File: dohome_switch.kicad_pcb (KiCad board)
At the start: 2 copper layers, 48.3 x 22.9 mm, 25 parts, among them P1 FTDI, P2 CONN_02X08, Q1 BSS138, Q2 BSS138, SW1 RST/PRG, U1 RT9013-33GB, U2 ESP-12E, U3 WS2812B

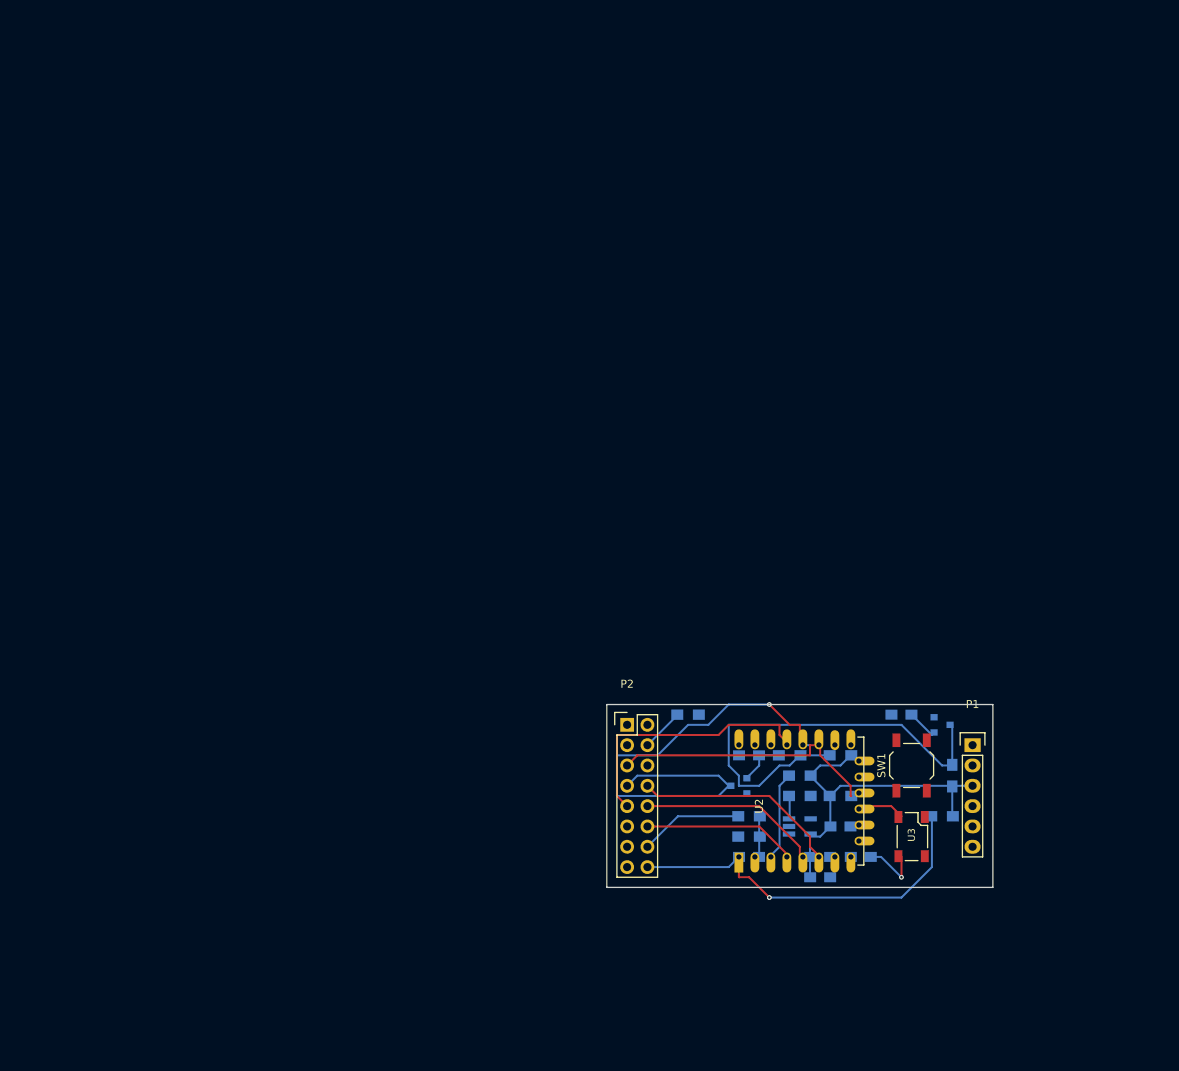
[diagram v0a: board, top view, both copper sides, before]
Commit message: CODE: new version with ftdi
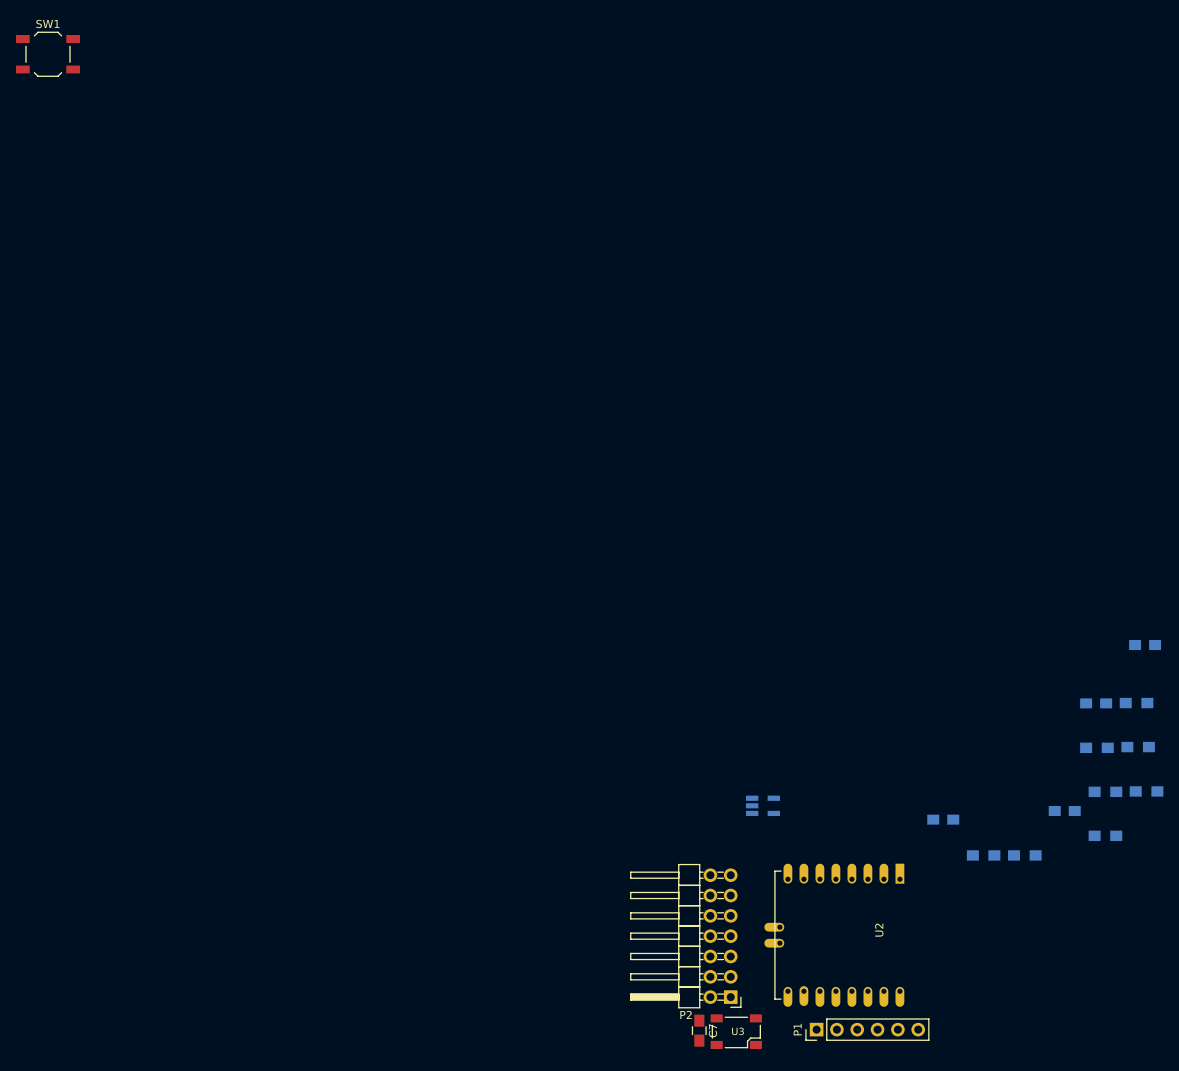
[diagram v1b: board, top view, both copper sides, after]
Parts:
- removed C3: 0.1uF, Capacitors_SMD:C_0805_HandSoldering
- removed C5: 2u2, Capacitors_SMD:C_0805_HandSoldering
- removed Q1, Q2: BSS138, TO_SOT_Packages_SMD:SOT-23
- removed R6: 470k, Resistors_SMD:R_0805_HandSoldering
- removed R7: 100k, Resistors_SMD:R_0805_HandSoldering
- C7: moved to F.Cu
- P1: footprint Pin_Headers:Pin_Header_Straight_1x06 -> Socket_Strips:Socket_Strip_Straight_1x06_Pitch2.54mm
- P2: value CONN_02X08 -> CONN_02X07; footprint Pin_Headers:Pin_Header_Straight_2x08 -> Pin_Headers:Pin_Header_Angled_2x07_Pitch2.54mm
- moved SW1 139.8 mm to (0.00, 0.00), turned to 0 degrees
- moved R10 54.3 mm to (132.2, 97.7)
- moved C2 49.9 mm to (137.1, 73.8)
- moved R9 49.9 mm to (136.3, 86.6)
- moved C1 47.4 mm to (131.0, 81.1)
- moved R2 43.4 mm to (137.3, 92.1)
- moved P1 40.6 mm to (96.1, 121.9), turned to 90 degrees
- moved R5 38.8 mm to (136.1, 81.1)
- moved P2 36.4 mm to (85.3, 117.9), turned to 180 degrees
- moved U3 32.8 mm to (86.0, 122.2), turned to 0 degrees
- moved R4 32.1 mm to (131.1, 86.7)
- moved R8 29.7 mm to (117.0, 100.1)
- moved C7 29.7 mm to (81.4, 122.0), turned to 270 degrees
- moved R1 29.1 mm to (122.1, 100.1)
- moved C6 28.1 mm to (127.1, 94.6)
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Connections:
- C1 pad 1: Net-(C1-Pad1) -> +5V
- C1 pad 2: Net-(C1-Pad2) -> GND
- C2 pad 2: Net-(C2-Pad2) -> GND
- C4 pad 2: Net-(C4-Pad2) -> GND
- C6 pad 2: Net-(C6-Pad2) -> GND
- C7 pad 1: Net-(C7-Pad1) -> +5V
- C7 pad 2: Net-(C7-Pad2) -> GND
- P1 pad 1: Net-(P1-Pad1) -> +3V3
- P1 pad 2: Net-(P1-Pad2) -> /GPIO0
- P1 pad 3: +3V3 -> /RXD
- P1 pad 4: /RXD -> /TXD
- P1 pad 5: /TXD -> GND
- P1 pad 6: Net-(P1-Pad6) -> /RESET
- P2 pad 1: Net-(P2-Pad1) -> GND
- P2 pad 11: /GPIO5 -> /GPIO12
- P2 pad 12: /GPIO16 -> /GPIO13
- P2 pad 13: /RXD -> +3V3
- P2 pad 14: /A0 -> +5V
- P2 pad 2: +3V3 -> /GPIO15
- P2 pad 3: Net-(P2-Pad3) -> /GPIO2
- P2 pad 4: /GPIO15 -> /GPIO0
- P2 pad 5: /GPIO2 -> /GPIO4
- P2 pad 6: /GPIO13 -> /GPIO5
- P2 pad 7: /GPIO0 -> /GPIO10
- P2 pad 8: /GPIO12 -> /A0
- P2 pad 9: /GPIO4 -> /GPIO16
- R1 pad 1: Net-(R1-Pad1) -> +5V
- R1 pad 2: Net-(R1-Pad2) -> GND
- R10 pad 2: Net-(R10-Pad2) -> GND
- R9 pad 2: Net-(R9-Pad2) -> GND
- SW1 pad 1: Net-(C3-Pad1) -> GND
- U1 pad 1: Net-(C1-Pad1) -> +5V
- U1 pad 2: Net-(U1-Pad2) -> GND
- U1 pad 3: Net-(R1-Pad1) -> +5V
- U1 pad 4: Net-(U1-Pad4) -> (no net)
- U2 pad 9: Net-(U2-Pad9) -> GND
- U3 pad 1: Net-(C7-Pad1) -> +5V
- U3 pad 2: Net-(U3-Pad2) -> (no net)
- U3 pad 3: Net-(U3-Pad3) -> GND
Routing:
- net /GPIO0: track 68.7 -> 0.00 mm, vias 1 -> 0
- net Net-(Q1-Pad3): track 52.8 -> 0.00 mm
- net /RESET: track 51.7 -> 0.00 mm, vias 1 -> 0
- net +3V3: track 45.2 -> 0.00 mm
- net /GPIO2: track 34.3 -> 0.00 mm
- net /GPIO4: track 33.7 -> 0.00 mm
- net /GPIO12: track 26.2 -> 0.00 mm
- net /GPIO14: track 22.8 -> 0.00 mm
- net /GPIO16: track 19.7 -> 0.00 mm
- net /A0: track 12.9 -> 0.00 mm
- net /CH_PD: track 11.5 -> 0.00 mm
- net Net-(C7-Pad1): track 7.81 -> 0.00 mm, vias 1 -> 0
- net /GPIO9: track 6.43 -> 0.00 mm
- net Net-(C5-Pad2): track 5.98 -> 0.00 mm
- net /ADC: track 5.86 -> 0.00 mm
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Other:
- board outline removed

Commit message: CODE: Without lines
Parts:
- removed SW1: RST/PRG, Buttons_Switches_SMD:SW_SPST_TL3342
- added JP1: JP1, Pin_Headers:Pin_Header_Straight_1x02_Pitch2.54mm, F.Cu at (89.3, 105.2)
- moved C1 51.4 mm to (88.3, 109.7), turned to 270 degrees
- moved C2 51.3 mm to (97.5, 106.4), turned to 90 degrees
- moved R5 48.5 mm to (100.2, 113.7), turned to 90 degrees
- moved R10 42.1 mm to (93.9, 115.3), turned to 180 degrees
- moved R2 40.2 mm to (99.8, 106.4), turned to 270 degrees
- moved R4 39.5 mm to (102.4, 113.7), turned to 90 degrees
- moved R9 37.8 mm to (103.9, 106.1)
- moved C6 35.3 mm to (96.1, 111.6), turned to 180 degrees
- moved R3 33.5 mm to (103.9, 110.2), turned to 180 degrees
- moved R1 33.2 mm to (90.4, 109.7), turned to 270 degrees
- moved C4 21.1 mm to (96.1, 109.7), turned to 180 degrees
- moved R8 15.2 mm to (103.9, 108.1)
- moved U1 13.0 mm to (93.9, 106.2)
- moved U2 0.89 mm to (107.4, 103.2)
- moved P1 0.71 mm to (96.8, 122.0)
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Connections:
- C1 pad 1: +5V -> /PWR
- C7 pad 1: +5V -> /PWR
- P1 pad 1: +3V3 -> /PWR
- P2 pad 14: +5V -> Net-(JP1-Pad2)
- R1 pad 1: +5V -> /PWR
- U1 pad 1: +5V -> /PWR
- U1 pad 3: +5V -> /PWR
- U3 pad 1: +5V -> /PWR

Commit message: CODE: first version
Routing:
- net GND: track 0.00 -> 32.0 mm, vias 0 -> 3
- net +3V3: track 0.00 -> 31.7 mm, vias 0 -> 1
- net /GPIO0: track 0.00 -> 29.7 mm, vias 0 -> 1
- net /PWR: track 0.00 -> 28.5 mm
- net /GPIO5: track 0.00 -> 25.5 mm
- net /RESET: track 0.00 -> 24.1 mm, vias 0 -> 1
- net /A0: track 0.00 -> 22.2 mm, vias 0 -> 1
- net /GPIO14: track 0.00 -> 21.5 mm
- net /GPIO16: track 0.00 -> 20.2 mm
- net /GPIO4: track 0.00 -> 19.9 mm
- net /GPIO2: track 0.00 -> 19.6 mm, vias 0 -> 1
- net /GPIO13: track 0.00 -> 18.4 mm
- net /GPIO12: track 0.00 -> 17.4 mm
- net /GPIO9: track 0.00 -> 16.2 mm, vias 0 -> 2
- net /GPIO15: track 0.00 -> 15.9 mm
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- added copper zone on B.Cu, net GND
- added copper zone on F.Cu, net GND

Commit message: CODE: new size of desk
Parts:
- moved R9 70.8 mm to (78.5, 40.1)
- moved C1 70.8 mm to (62.9, 43.7)
- moved C7 70.8 mm to (56.5, 56.3)
- moved JP1 70.8 mm to (63.9, 39.2)
- moved P1 70.8 mm to (71.4, 56.0)
- moved R1 70.8 mm to (65.0, 43.7)
- moved R10 70.8 mm to (68.5, 49.2)
- moved R3 70.8 mm to (78.5, 44.1)
- moved R5 70.8 mm to (74.8, 47.7)
- moved R8 70.8 mm to (78.5, 42.0)
- moved U1 70.8 mm to (68.5, 40.1)
- moved U2 70.8 mm to (82.0, 37.1)
- moved U3 70.8 mm to (61.2, 56.3)
- moved C2 70.8 mm to (72.1, 40.4)
- moved C4 70.8 mm to (70.7, 43.7)
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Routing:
- net /PWR: track 28.5 -> 45.6 mm, vias 0 -> 1
- net GND: track 32.0 -> 42.8 mm
- net /GPIO15: track 15.9 -> 17.9 mm, vias 0 -> 1
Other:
- board outline added: 32.8 x 25.3 mm
